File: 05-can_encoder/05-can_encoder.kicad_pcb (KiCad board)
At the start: 2 copper layers, 25.4 x 25.4 mm, 23 parts, among them IC1 STM32F072CBT6, IC2 AS5047P-ATSM, J1 Conn_02x05_Odd_Even, U1 SN65HVD230DR, U2 LM3940IMPX-3.3_NOPB

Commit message: wip layout diff pair
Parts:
- added R2: 120, Resistor_SMD:R_0603_1608Metric, F.Cu at (202.3, 47.9)
- moved C11 2.07 mm to (199.9, 58.4)
- moved U1 2.07 mm to (200.1, 53.8)
- moved C8 0.66 mm to (212.8, 47.4)
- moved C7 0.65 mm to (215.0, 48.1)
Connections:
- net USB_DM renamed USB_D-
- net USB_DP renamed USB_D+
- J1 pad 3: CAN_L -> CAN+
- J1 pad 4: CAN_H -> CAN+
- J1 pad 5: CAN_L -> CAN-
- J1 pad 6: CAN_H -> CAN-
- U1 pad 6: CAN_L -> CAN-
- U1 pad 7: CAN_H -> CAN+
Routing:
- net CAN-: track 0.00 -> 14.8 mm
- net CAN+: track 0.00 -> 14.4 mm
- net CAN_H: track 13.6 -> 0.00 mm
- net CAN_L: track 10.5 -> 0.00 mm
- net USB_D-: track 10.9 -> 13.4 mm
- net can_rx: track 13.0 -> 11.6 mm
- net can_tx: track 19.7 -> 20.8 mm
- net 3v3: track 20.4 -> 21.0 mm

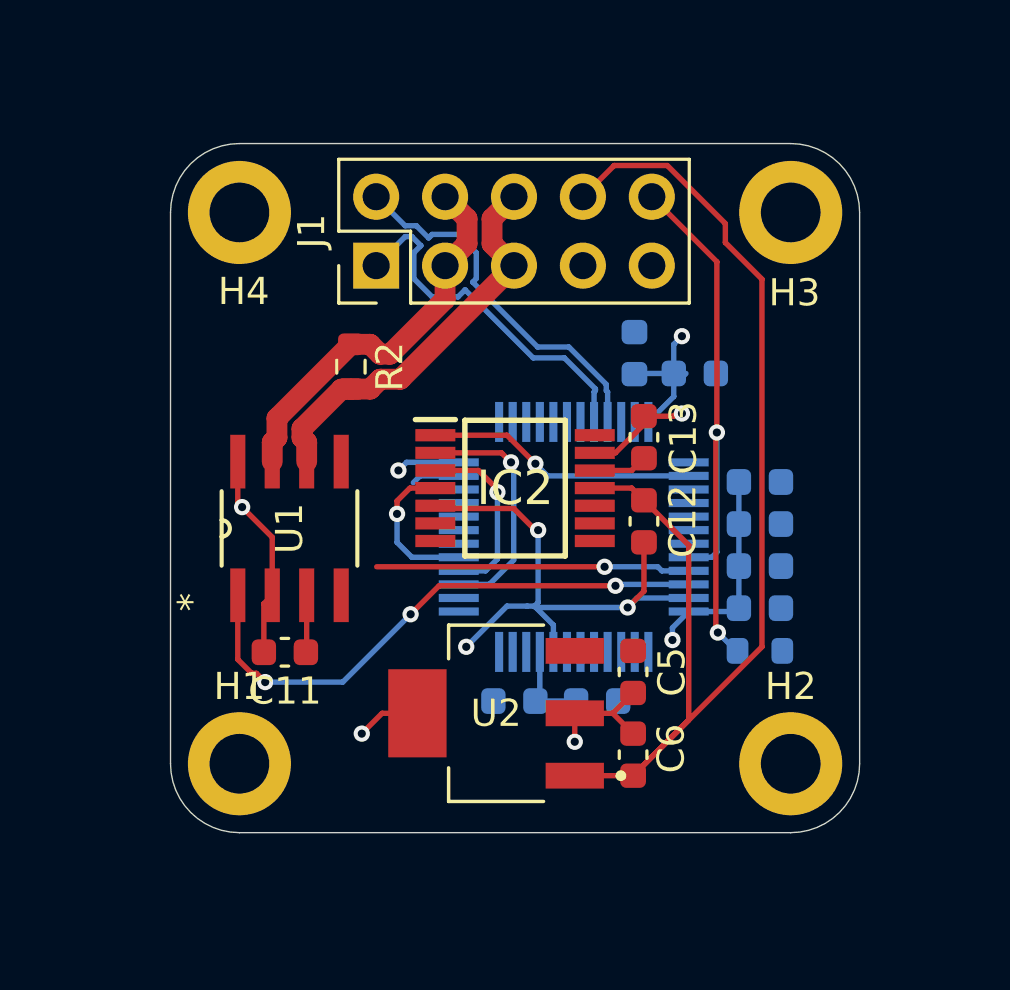
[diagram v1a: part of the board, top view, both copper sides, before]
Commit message: layout fixes
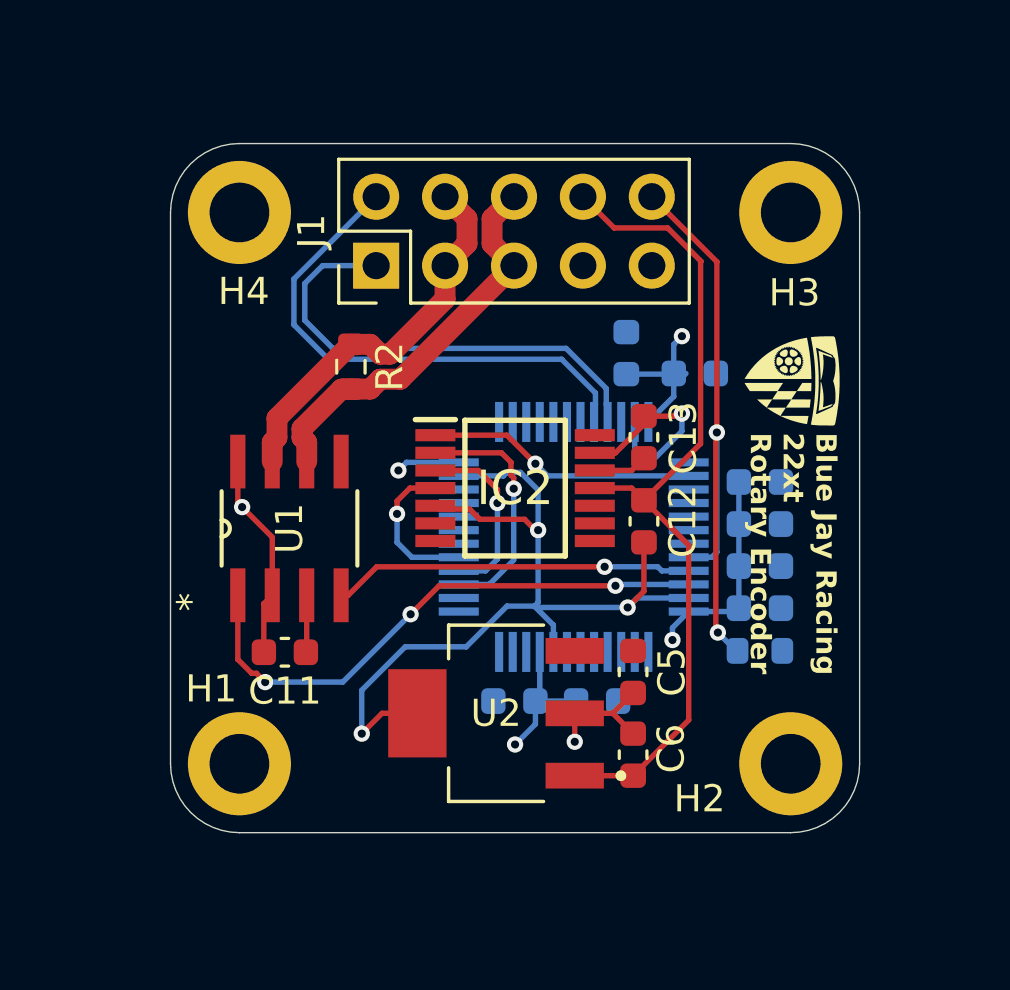
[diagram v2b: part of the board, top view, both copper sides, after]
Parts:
- added G***: BJR_LOGO, can_encoder:BJR_LOGO, F.Cu at (218.6, 48.4)
- R2: value 120 -> 60
- moved C8 0.30 mm to (212.5, 47.4)
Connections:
- J1 pad 1: USB_D- -> USB_D+
- J1 pad 2: USB_D+ -> USB_D-
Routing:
- net 5v: track 45.3 -> 30.9 mm
- net GND: track 40.9 -> 54.0 mm, vias 7 -> 6
- net USB_D-: track 13.4 -> 19.2 mm
- net USB_D+: track 13.7 -> 17.7 mm
- net 3v3: track 21.0 -> 23.2 mm, vias 3 -> 4
- net can_rx: track 11.6 -> 13.3 mm
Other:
- board text added: "Blue Jay Racing 22xt Rotary Encoder"
- board text added: "Cyan Brown"
- board text added: "Emma Ouyang Justin Wang"
